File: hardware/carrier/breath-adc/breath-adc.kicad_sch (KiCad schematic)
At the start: 9 parts

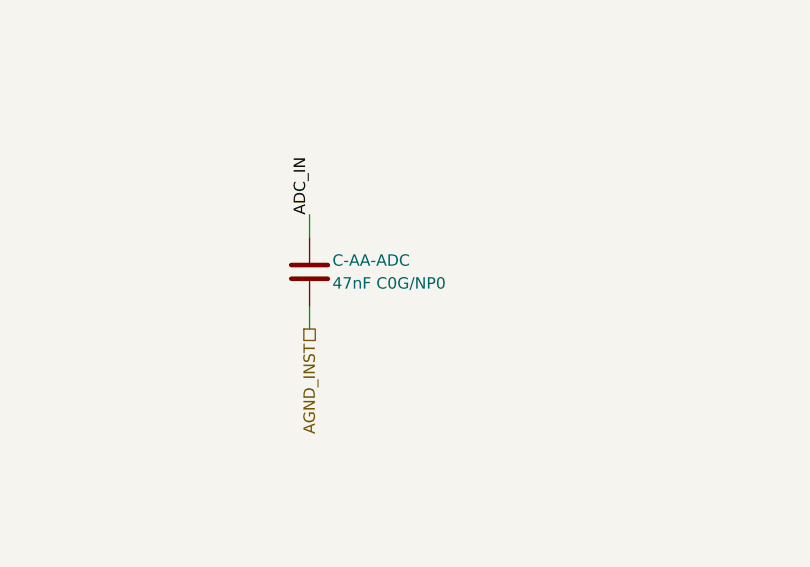
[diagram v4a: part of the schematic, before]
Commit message: #32: checkpoint — switchable breath band-limit, 1.5 kHz ADC filter, breath LED
Receive stage: C_diff switched by U-BW-SW (TMUX6112) from SW-BREATH-BW
(NKK M2024, left 500 Hz / centre 1.5 kHz / right WIDE): 680 pF fixed,
3.9 nF and 10 nF switched; C_cm 68 pF matched pair. C-OUT-BREATH 10 nF C0G.
C-AA-ADC 18 nF (1.47 kHz), sample rate kept at 4 kHz. Breath LED driver on
U-REF-BUF B. Sheets, BOM fragments, datasheets (TMUX6112, MMBT3904), sims,
ADR 0003/0004 amendments, pages. Sims still being re-run.

Gate-Red: sims stale while re-running (breath-receive-stage, breath-output-stage, interfaces/system, pitch-stage); breath-sense-link/sim pg_gain_max < 1e-3 fails in every mode and power-entry/sim led-pwm breath_mv fails at 2 kHz - both consequences of #32 left for the owner, not loosened; breath-receive-stage cmrr-wide fails 58.5 dB above ~7.4 kHz (owner); kicad: module-main and main-board .kicad_pcb parity broken by the new/changed parts (re-placement is the module re-layout's; pcb not touched), plus module-main's pre-existing routing failures

Co-Authored-By: Claude Opus 5.5 <noreply@anthropic.com>
Claude-Session: https://claude.ai/code/session_01LmB4muFXnoLprWX4JzuJ5A
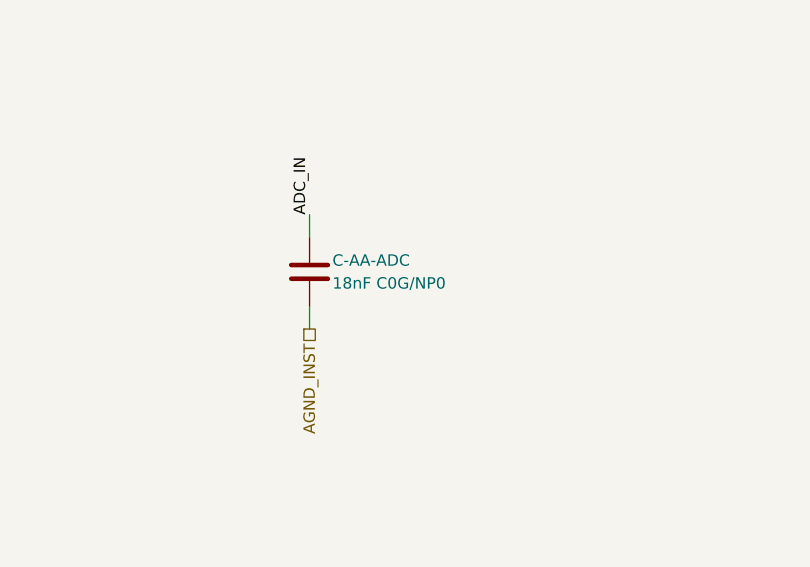
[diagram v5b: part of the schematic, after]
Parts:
- C-AA-ADC: value 47nF C0G/NP0 -> 18nF C0G/NP0; LCSC C22402129 -> C3848365; MPN C0805C473J3GACTU -> GRM2165C1H183JA01D; Manufacturer KEMET -> Murata
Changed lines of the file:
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@@
     (in_bom yes) (on_board yes) (dnp no)
     (property "Reference" "C-AA-ADC" (at 144.78 49.53 0) (effects (font (size 1.27 1.27)) (justify left)))
-    (property "Value" "47nF C0G/NP0" (at 144.78 52.07 0) (effects (font (size 1.27 1.27)) (justify left)))
+    (property "Value" "18nF C0G/NP0" (at 144.78 52.07 0) (effects (font (size 1.27 1.27)) (justify left)))
     (property "Footprint" "Capacitor_SMD:C_0805_2012Metric" (at 143.51 54.61 0) (effects (font (size 1.27 1.27)) hide))
     (property "Datasheet" "" (at 142.24 50.8 0) (effects (font (size 1.27 1.27)) hide))
@@
     (property "Pins" "1=1 2=2" (at 142.24 50.8 0) (effects (font (size 1.27 1.27)) hide))
     (property "Note" "Anti-alias at the divider node. It has to settle inside the sample window, which is what stops the upper leg going higher still" (at 142.24 50.8 0) (effects (font (size 1.27 1.27)) hide))
-    (property "Manufacturer" "KEMET" (at 142.24 50.8 0) (effects (font (size 1.27 1.27)) hide))
-    (property "MPN" "C0805C473J3GACTU" (at 142.24 50.8 0) (effects (font (size 1.27 1.27)) hide))
-    (property "LCSC" "C22402129" (at 142.24 50.8 0) (effects (font (size 1.27 1.27)) hide))
+    (property "Manufacturer" "Murata" (at 142.24 50.8 0) (effects (font (size 1.27 1.27)) hide))
+    (property "MPN" "GRM2165C1H183JA01D" (at 142.24 50.8 0) (effects (font (size 1.27 1.27)) hide))
+    (property "LCSC" "C3848365" (at 142.24 50.8 0) (effects (font (size 1.27 1.27)) hide))
     (property "Assembly" "machine" (at 142.24 50.8 0) (effects (font (size 1.27 1.27)) hide))
     (pin "1")
